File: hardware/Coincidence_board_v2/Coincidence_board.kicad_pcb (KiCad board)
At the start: 2 copper layers, 136.8 x 85 mm, 74 parts, among them J1 Inputs, J2 chan2_in, J3 POWER_IN, J4 Morpho_Gauche, J5 chan3_out, J7 Morpho_Droite, SW1 SW_1, U1 74HCT74, U2 74HCT74, U3 LM7805_TO220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

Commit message: Update Coincidence Board / v2
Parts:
- removed ? (x2): , 
- removed D2, D3, D4, D5, D6, D7: 1N4148, Diode_THT:D_DO-35_SOD27_P7.62mm_Horizontal
- removed J4: Morpho_Gauche, Connector_PinHeader_2.54mm:PinHeader_2x20_P2.54mm_Vertical
- removed J7: Morpho_Droite, Connector_PinHeader_2.54mm:PinHeader_2x20_P2.54mm_Vertical
- added U8: NUCLEO-L432KC, NUCLEO_L432KC:MODULE_NUCLEO-L432KC, F.Cu at (196.6, 122.9)
- U1, U2, U4, U5, U6, U7: footprint Package_SO:SO-14_3.9x8.65mm_P1.27mm -> Package_DIP:DIP-14_W7.62mm_Socket_LongPads
- moved R10 228.4 mm to (25.8, 133.3), turned to 0 degrees
- moved R2 215.7 mm to (25.8, 100.9), turned to 0 degrees
- moved R9 210.6 mm to (25.8, 129.3), turned to 0 degrees
- moved R11 205.6 mm to (52.5, 49.1)
- moved U5 203.5 mm to (41.0, 46.6)
- moved R15 201.9 mm to (39.1, 109.0), turned to 0 degrees
- moved R29 198.8 mm to (52.4, 121.2), turned to 0 degrees
- moved J1 188.1 mm to (66.5, 129.1), turned to 0 degrees
- moved C14 187.2 mm to (66.0, 110.8), turned to 0 degrees
- moved R21 186.7 mm to (33.0, 59.2), turned to -90 degrees
- moved R30 185.3 mm to (52.4, 125.2), turned to 0 degrees
- moved R14 184.7 mm to (39.1, 105.0), turned to 0 degrees
- moved R16 182.7 mm to (39.1, 113.1), turned to 0 degrees
- moved R28 182.4 mm to (52.4, 117.1)
- moved R17 178.6 mm to (39.1, 117.1), turned to 0 degrees
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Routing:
- net 5V: track 396.7 -> 0.00 mm, vias 5 -> 0
- net 3.3V_NUC: track 130.3 -> 0.00 mm
- net A2in: track 121.0 -> 0.00 mm, vias 2 -> 0
- net GND: track 105.8 -> 0.00 mm, vias 6 -> 0
- net VIN: track 101.6 -> 0.00 mm
- net Net-(U4A-C): track 91.9 -> 0.00 mm
- net Net-(U4B-~{Q}): track 77.7 -> 0.00 mm, vias 5 -> 0
- net C2in: track 74.8 -> 0.00 mm, vias 1 -> 0
- net BC2out: track 72.4 -> 0.00 mm, vias 2 -> 0
- net Net-(U4B-Q): track 70.4 -> 0.00 mm, vias 2 -> 0
- net AB2out: track 66.1 -> 0.00 mm, vias 1 -> 0
- net Ain: track 66.1 -> 0.00 mm, vias 1 -> 0
- net AB2out_nuc: track 61.3 -> 0.00 mm
- net B2in: track 53.9 -> 0.00 mm, vias 1 -> 0
- net A2out_nuc: track 46.2 -> 0.00 mm
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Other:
- board text added: "Nucleo G431KB"
- board text removed: "A"
- board text removed: "AB"
- board text removed: "AC"
- board text removed: "B"
- board text removed: "BC"
- board text removed: "IN"
- board text removed: "K"
- board text removed: "Nucleo L476RG"
- board text removed: "OUT"
- board text removed: "X"

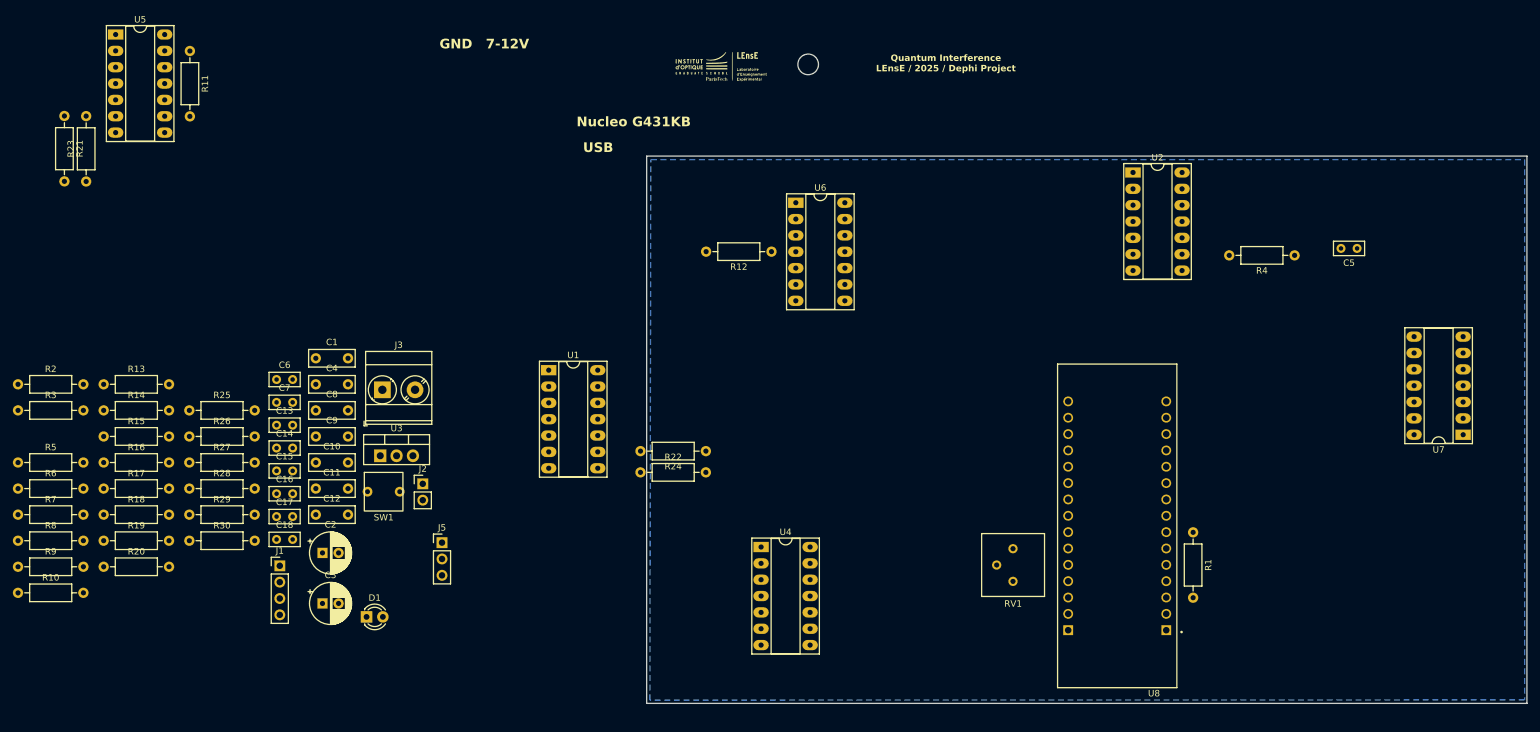
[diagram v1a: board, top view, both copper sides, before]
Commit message: Update GRA experiment / Creating new electronic interface based on G431KB Nucleo board
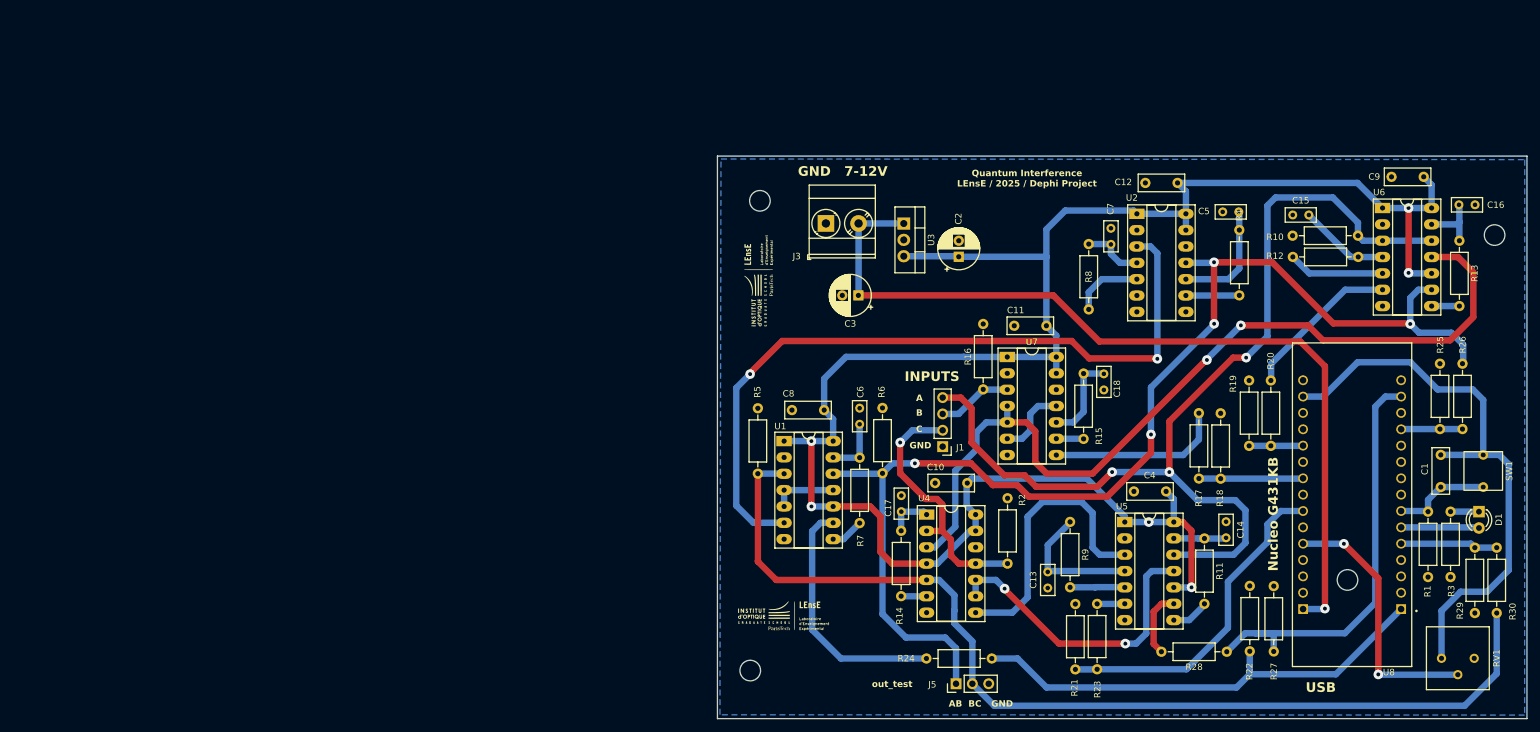
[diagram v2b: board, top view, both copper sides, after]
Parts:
- removed the G*** at (135.1, 51.3)
- removed J2: chan2_in, Connector_PinHeader_2.54mm:PinHeader_1x02_P2.54mm_Vertical
- added ?: , , F.Cu at (232.4, 131.3)
- added ?: , , F.Cu at (255.3, 77.7)
- added G***: LOGO, LEnsE:Logo_Small, F.Cu at (144.8, 136.7)
- added G***: LOGO, LEnsE:Logo_Small, F.Cu at (140.7, 84.8)
- added M: MountingHole_3.2mm_M3, MountingHole:MountingHole_3.2mm_M3, F.Cu at (141.1, 72.4)
- J5: value chan3_out -> test_out
- moved R3 223.2 mm to (248.4, 120.7), turned to -90 degrees
- moved R10 215.5 mm to (234.0, 77.8), turned to 180 degrees
- moved R13 211.9 mm to (249.8, 78.6), turned to -90 degrees
- moved R30 203.2 mm to (255.6, 126.3), turned to -90 degrees
- moved R29 200.4 mm to (252.2, 136.5), turned to 90 degrees
- moved R26 197.9 mm to (250.3, 107.9), turned to 90 degrees
- moved R25 194.5 mm to (246.8, 97.7), turned to -90 degrees
- moved C16 191.6 mm to (252.2, 73.0), turned to 180 degrees
- moved R20 182.4 mm to (220.5, 110.5), turned to 90 degrees
- moved R19 179.7 mm to (217.1, 100.3), turned to -90 degrees
- moved C1 175.5 mm to (246.9, 111.9), turned to -90 degrees
- moved R11 174.9 mm to (210.2, 124.9)
- moved R21 174.4 mm to (190.1, 135.1)
- moved R23 174.4 mm to (193.5, 145.2)
- moved R18 174.3 mm to (212.7, 105.4), turned to -90 degrees
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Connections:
- J1 pad 2: A2in -> C2in
- J1 pad 4: C2in -> A2in
- J5 pad 1: AC2out -> AB2out
- J5 pad 2: AB2out -> BC2out
- J5 pad 3: BC2out -> GND
- R5 pad 1: Bin -> BC2out
- R6 pad 2: Ain -> AB2out
- U1 pad 12: Ain -> AB2out
- U1 pad 3: Bin -> BC2out
- U2 pad 11: Ain -> AB2out
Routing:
- net 5V: track 0.00 -> 300.3 mm, vias 0 -> 6
- net AB2out: track 0.00 -> 189.2 mm, vias 0 -> 5
- net BC2out: track 0.00 -> 159.8 mm
- net A2in: track 0.00 -> 155.2 mm, vias 0 -> 3
- net VIN: track 0.00 -> 136.4 mm, vias 0 -> 1
- net Net-(U4A-C): track 0.00 -> 134.8 mm, vias 0 -> 2
- net Net-(U1A-~{Q}): track 0.00 -> 116.5 mm, vias 0 -> 2
- net 3.3V_NUC: track 0.00 -> 89.2 mm
- net ABCout_nuc: track 0.00 -> 74.1 mm
- net AC2out_nuc: track 0.00 -> 67.0 mm
- net C2out_nuc: track 0.00 -> 51.4 mm
- net Net-(U4B-Q): track 0.00 -> 47.3 mm, vias 0 -> 2
- net Net-(U4B-~{Q}): track 0.00 -> 44.2 mm
- net POT_OUT: track 0.00 -> 41.2 mm, vias 0 -> 2
- net C2in: track 0.00 -> 41.0 mm, vias 0 -> 1
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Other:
- board size 136.8 x 85 mm -> 125.8 x 87.4 mm
- board text added: "A"
- board text added: "AB"
- board text added: "B"
- board text added: "BC"
- board text added: "C"
- board text added: "INPUTS"
- board text added: "out_test"

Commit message: Update Board v2 / Before sending to JLCPCB
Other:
- rule pad_to_mask_clearance: 0.05 -> 0
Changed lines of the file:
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@@
 	)
 	(setup
-		(pad_to_mask_clearance 0.05)
-		(solder_mask_min_width 0.25)
+		(pad_to_mask_clearance 0)
 		(allow_soldermask_bridges_in_footprints no)
 		(pcbplotparams
@@
 		(at 144.801933 136.673425)
 		(property "Reference" "G***"
-			(at 0 0 360)
+			(at 0 0 0)
 			(layer "F.SilkS")
 			(hide yes)
@@
 		)
 		(property "Value" "LOGO"
-			(at 0.75 0 360)
+			(at 0.75 0 0)
 			(layer "F.SilkS")
 			(hide yes)
@@
 		(tags "Resistor Axial_DIN0207 series Axial Horizontal pin pitch 10.16mm 0.25W = 1/4W length 6.3mm diameter 2.5mm")
 		(property "Reference" "R17"
-			(at -3.058 -0.024 270)
+			(at -3.058 -0.024 -90)
 			(layer "F.SilkS")
 			(effects
@@
 		)
 		(property "Value" "2.2k"
-			(at 5.08 2.37 270)
+			(at 5.08 2.37 -90)
 			(layer "F.Fab")
 			(effects
@@
 		)
 		(fp_text user "${REFERENCE}"
-			(at 5.08 0 270)
+			(at 5.08 0 -90)
 			(layer "F.Fab")
 			(effects
@@
 		(tags "C Rect series Radial pin pitch 2.50mm  length 4.6mm width 2mm Capacitor")
 		(property "Reference" "C5"
-			(at -2.92 -0.1 360)
+			(at -2.92 -0.1 0)
 			(layer "F.SilkS")
 			(effects
@@
 		)
 		(property "Value" "220pF"
-			(at 1.25 2.25 360)
+			(at 1.25 2.25 0)
 			(layer "F.Fab")
 			(effects
@@
 		)
 		(fp_text user "${REFERENCE}"
-			(at 1.25 0 360)
+			(at 1.25 0 0)
 			(layer "F.Fab")
 			(effects
@@
 		(tags "Resistor Axial_DIN0207 series Axial Horizontal pin pitch 10.16mm 0.25W = 1/4W length 6.3mm diameter 2.5mm")
 		(property "Reference" "R29"
-			(at 0.36 -2.3 270)
+			(at 0.36 -2.3 -90)
 			(layer "F.SilkS")
 			(effects
@@
 		)
 		(property "Value" "3.3k"
-			(at 5.08 2.37 270)
+			(at 5.08 2.37 -90)
 			(layer "F.Fab")
 			(effects
@@
 		)
 		(fp_text user "${REFERENCE}"
-			(at 5.08 0 270)
+			(at 5.08 0 -90)
 			(layer "F.Fab")
 			(effects
@@
 		(tags "CP Radial series Radial pin pitch 2.50mm  diameter 6.3mm Electrolytic Capacitor")
 		(property "Reference" "C2"
-			(at 5.916 -0.042 270)
+			(at 5.916 -0.042 -90)
 			(layer "F.SilkS")
 			(effects
@@
 		)
 		(property "Value" "100uF"
-			(at 1.25 4.4 270)
+			(at 1.25 4.4 -90)
 			(layer "F.Fab")
 			(effects
@@
 		)
 		(fp_text user "${REFERENCE}"
-			(at 1.25 0 270)
+			(at 1.25 0 -90)
 			(layer "F.Fab")
 			(effects
@@
 		(tags "Resistor Axial_DIN0207 series Axial Horizontal pin pitch 10.16mm 0.25W = 1/4W length 6.3mm diameter 2.5mm")
 		(property "Reference" "R5"
-			(at 12.692 -0.064 270)
+			(at 12.692 -0.064 -90)
 			(layer "F.SilkS")
 			(effects
@@
 		)
 		(property "Value" "50"
-			(at 5.08 2.37 270)
+			(at 5.08 2.37 -90)
 			(layer "F.Fab")
 			(effects
@@
 		)
 		(fp_text user "${REFERENCE}"
-			(at 5.08 0 270)
+			(at 5.08 0 -90)
 			(layer "F.Fab")
 			(effects
@@
 		(tags "Resistor Axial_DIN0207 series Axial Horizontal pin pitch 10.16mm 0.25W = 1/4W length 6.3mm diameter 2.5mm")
 		(property "Reference" "R2"
-			(at 9.906 2.286 270)
+			(at 9.906 2.286 -90)
 			(layer "F.SilkS")
 			(effects
@@
 		)
 		(property "Value" "50"
-			(at 5.08 2.37 270)
+			(at 5.08 2.37 -90)
 			(layer "F.Fab")
 			(effects
@@
 		)
 		(fp_text user "${REFERENCE}"
-			(at 24.66 -21.32 270)
+			(at 24.66 -21.32 -90)
 			(layer "F.Fab")
 			(effects
@@
 		(tags "Resistor Axial_DIN0207 series Axial Horizontal pin pitch 10.16mm 0.25W = 1/4W length 6.3mm diameter 2.5mm")
 		(property "Reference" "R20"
-			(at 13.198 -0.028 270)
+			(at 13.198 -0.028 -90)
 			(layer "F.SilkS")
 			(effects
@@
 		)
 		(property "Value" "2.2k"
-			(at 5.08 2.37 270)
+			(at 5.08 2.37 -90)
 			(layer "F.Fab")
 			(effects
@@
 		)
 		(fp_text user "${REFERENCE}"
-			(at 5.08 0 270)
+			(at 5.08 0 -90)
 			(layer "F.Fab")
 			(effects
@@
 		)
 		(property "Value" "test_out"
-			(at 0 7.41 270)
+			(at 0 7.41 -90)
 			(layer "F.Fab")
 			(effects
@@
 		)
 		(fp_text user "${REFERENCE}"
-			(at 0 2.54 360)
+			(at 0 2.54 0)
 			(layer "F.Fab")
 			(effects
@@
 		(tags "C Rect series Radial pin pitch 5.00mm  length 7mm width 2.5mm Capacitor")
 		(property "Reference" "C11"
-			(at 0.228 -2.412 360)
+			(at 0.228 -2.412 0)
 			(layer "F.SilkS")
 			(effects
@@
 		)
 		(property "Value" "100nF"
-			(at 2.5 2.5 360)
+			(at 2.5 2.5 0)
 			(layer "F.Fab")
 			(effects
@@
 		)
 		(fp_text user "${REFERENCE}"
-			(at 2.5 0 360)
+			(at 2.5 0 0)
 			(layer "F.Fab")
 			(effects
@@
 		(at 140.694067 84.814575 90)
 		(property "Reference" "G***"
-			(at 0 0 270)
+			(at 0 0 -90)
 			(layer "F.SilkS")
 			(hide yes)
@@
 		)
 		(property "Value" "LOGO"
-			(at 0.75 0 270)
+			(at 0.75 0 -90)
 			(layer "F.SilkS")
 			(hide yes)
@@
 		(tags "Resistor Axial_DIN0207 series Axial Horizontal pin pitch 10.16mm 0.25W = 1/4W length 6.3mm diameter 2.5mm")
 		(property "Reference" "R16"
-			(at 5.08 -2.37 270)
+			(at 5.08 -2.37 -90)
 			(layer "F.SilkS")
 			(effects
@@
 		)
 		(property "Value" "50"
-			(at 5.08 2.37 270)
+			(at 5.08 2.37 -90)
 			(layer "F.Fab")
 			(effects
@@
 		)
 		(fp_text user "${REFERENCE}"
-			(at 5.08 0 270)
+			(at 5.08 0 -90)
 			(layer "F.Fab")
 			(effects
@@
 		(tags "Resistor Axial_DIN0207 series Axial Horizontal pin pitch 10.16mm 0.25W = 1/4W length 6.3mm diameter 2.5mm")
 		(property "Reference" "R26"
-			(at 13.085 0.025 270)
+			(at 13.085 0.025 -90)
 			(layer "F.SilkS")
 			(effects
@@
 		)
 		(property "Value" "2.2k"
-			(at 5.08 2.37 270)
+			(at 5.08 2.37 -90)
 			(layer "F.Fab")
 			(effects
@@
 		)
 		(fp_text user "${REFERENCE}"
-			(at 5.08 0 270)
+			(at 5.08 0 -90)
 			(layer "F.Fab")
 			(effects
@@
 		(tags "C Rect series Radial pin pitch 2.50mm  length 4.6mm width 2mm Capacitor")
 		(property "Reference" "C18"
-			(at 0.19 2.046 270)
+			(at 0.19 2.046 -90)
 			(layer "F.SilkS")
 			(effects
@@
 		)
 		(property "Value" "220pF"
-			(at 1.25 2.25 270)
+			(at 1.25 2.25 -90)
 			(layer "F.Fab")
 			(effects
@@
 		)
 		(fp_text user "${REFERENCE}"
-			(at 1.25 0 270)
+			(at 1.25 0 -90)
 			(layer "F.Fab")
 			(effects
@@
 		(tags "THT DIP DIL PDIP 2.54mm 7.62mm 300mil Socket LongPads")
 		(property "Reference" "U7"
-			(at 3.81 -2.33 360)
+			(at 3.81 -2.33 0)
 			(layer "F.SilkS")
 			(effects
@@
 		)
 		(property "Value" "74HC74"
-			(at 3.81 17.57 360)
+			(at 3.81 17.57 0)
 			(layer "F.Fab")
 			(effects
@@
 		)
 		(fp_text user "${REFERENCE}"
-			(at 3.81 7.62 360)
+			(at 3.81 7.62 0)
 			(layer "F.Fab")
 			(effects
@@
 		(tags "C Rect series Radial pin pitch 2.50mm  length 4.6mm width 2mm Capacitor")
 		(property "Reference" "C13"
-			(at 1.25 -2.25 270)
+			(at 1.25 -2.25 -90)
 			(layer "F.SilkS")
 			(effects
@@
 		)
 		(property "Value" "220pF"
-			(at 1.41 6.19 270)
+			(at 1.41 6.19 -90)
 			(layer "F.Fab")
 			(effects
@@
 		)
 		(fp_text user "${REFERENCE}"
-			(at 1.25 0 270)
+			(at 1.25 0 -90)
 			(layer "F.Fab")
 			(effects
@@
 		)
 		(fp_text user "${REFERENCE}"
-			(at 0 3.81 270)
+			(at 0 3.81 -90)
 			(layer "F.Fab")
 			(effects
@@
 		(start 156.435 75.917623)
 		(end 156.435 87.065)
-		(width 1)
+		(width 1.5)
 		(layer "B.Cu")
 		(net 4)
@@
 		(start 156.435 75.917623)
 		(end 163.44 75.917623)
-		(width 1)
+		(width 1.5)
 		(layer "B.Cu")
 		(net 4)
@@
 		(start 185.62 81.11)
 		(end 185.62 76.85)
-		(width 1)
+		(width 1.5)
 		(layer "B.Cu")
 		(net 36)
@@
 		(start 185.62 76.85)
 		(end 188.556 73.914)
-		(width 1)
+		(width 1.5)
 		(layer "B.Cu")
 		(net 36)
@@
 		(start 163.455 81.012623)
 		(end 171.912623 81.012623)
-		(width 1)
+		(width 1.5)
 		(layer "B.Cu")
 		(net 36)
@@
 		(start 172 81.1)
 		(end 185.61 81.1)
-		(width 1)
+		(width 1.5)
 		(layer "B.Cu")
 		(net 36)
@@
 		(start 188.556 73.914)
 		(end 199.174 73.914)
-		(width 1)
+		(width 1.5)
 		(layer "B.Cu")
 		(net 36)
@@
 		(start 185.62 91.82)
 		(end 185.62 81.11)
-		(width 1)
+		(width 1.5)
 		(layer "B.Cu")
 		(net 36)
